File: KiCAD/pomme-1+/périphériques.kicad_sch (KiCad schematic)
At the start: 19 parts, among them J1 DE9_female, J2 5V MCU UART, J3 close to use IRQ on ACIA, J4 rs232-socket, J5 rs232-plug, Q3 2N3904, U10 MAX232CPE

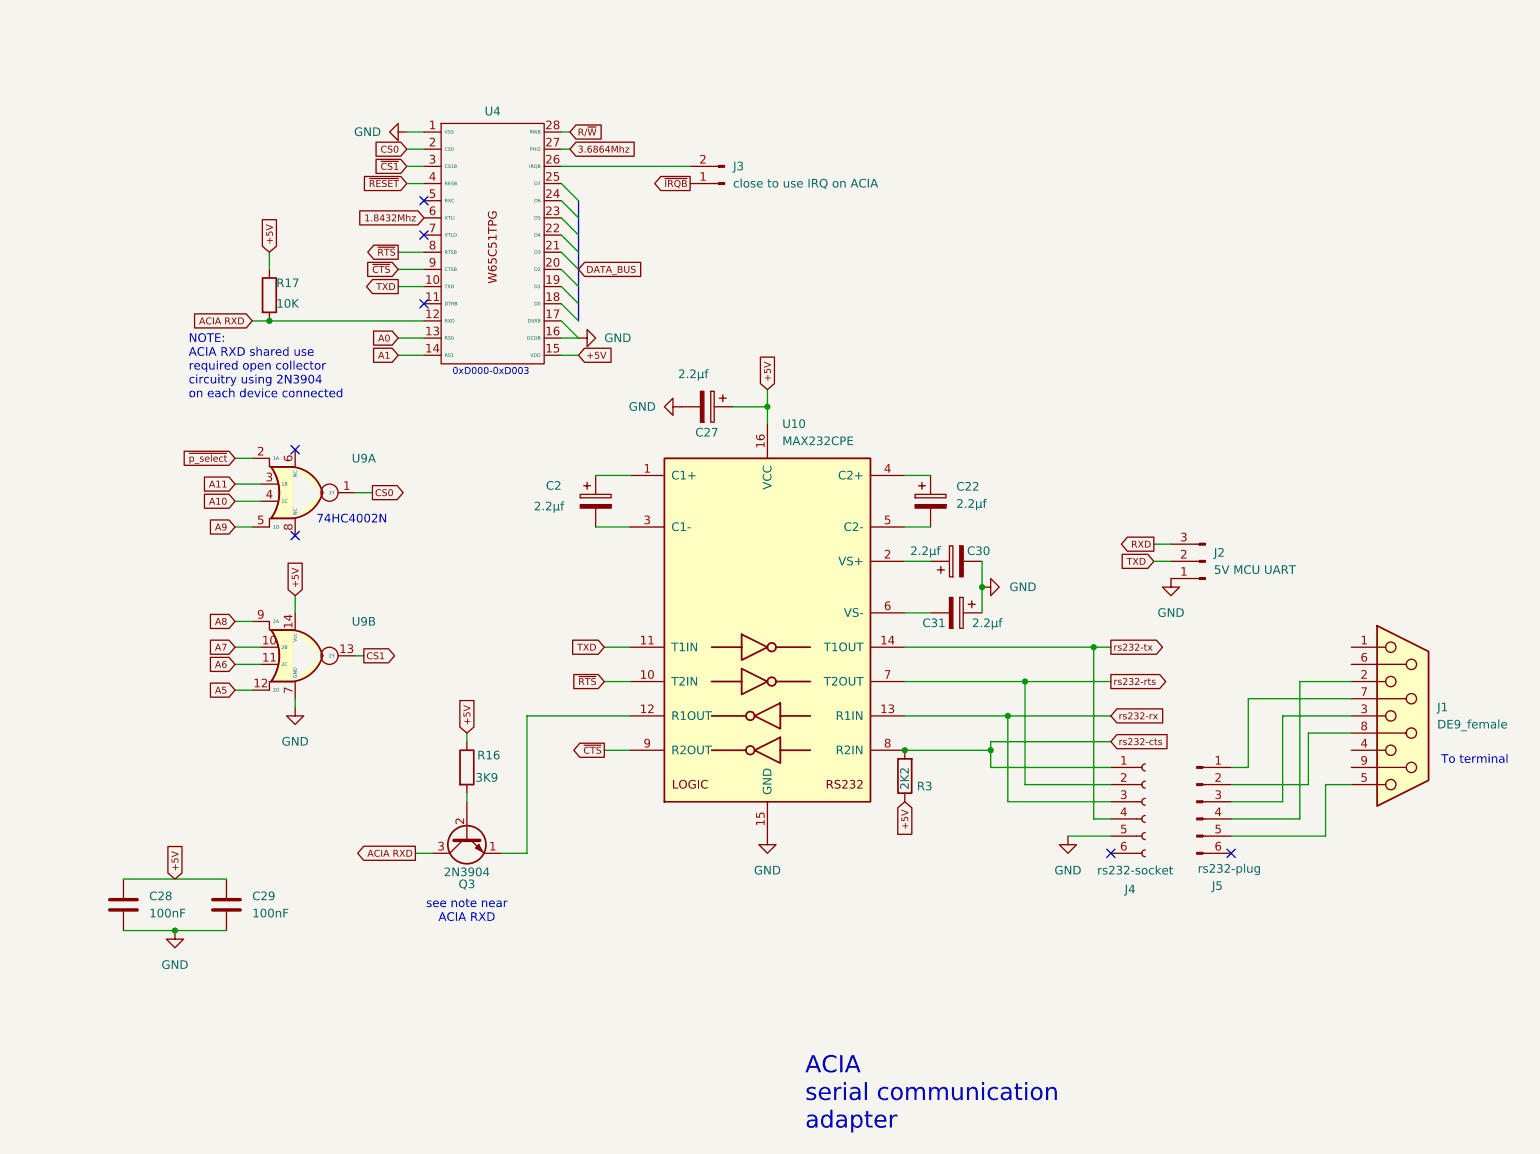
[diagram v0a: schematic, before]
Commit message: Modification de la conception du pomme 1+ Ajout d'un PIA W65C22 à la carte périphériques Ajout d'un régulateur de tension 3.3V à l'alimentation
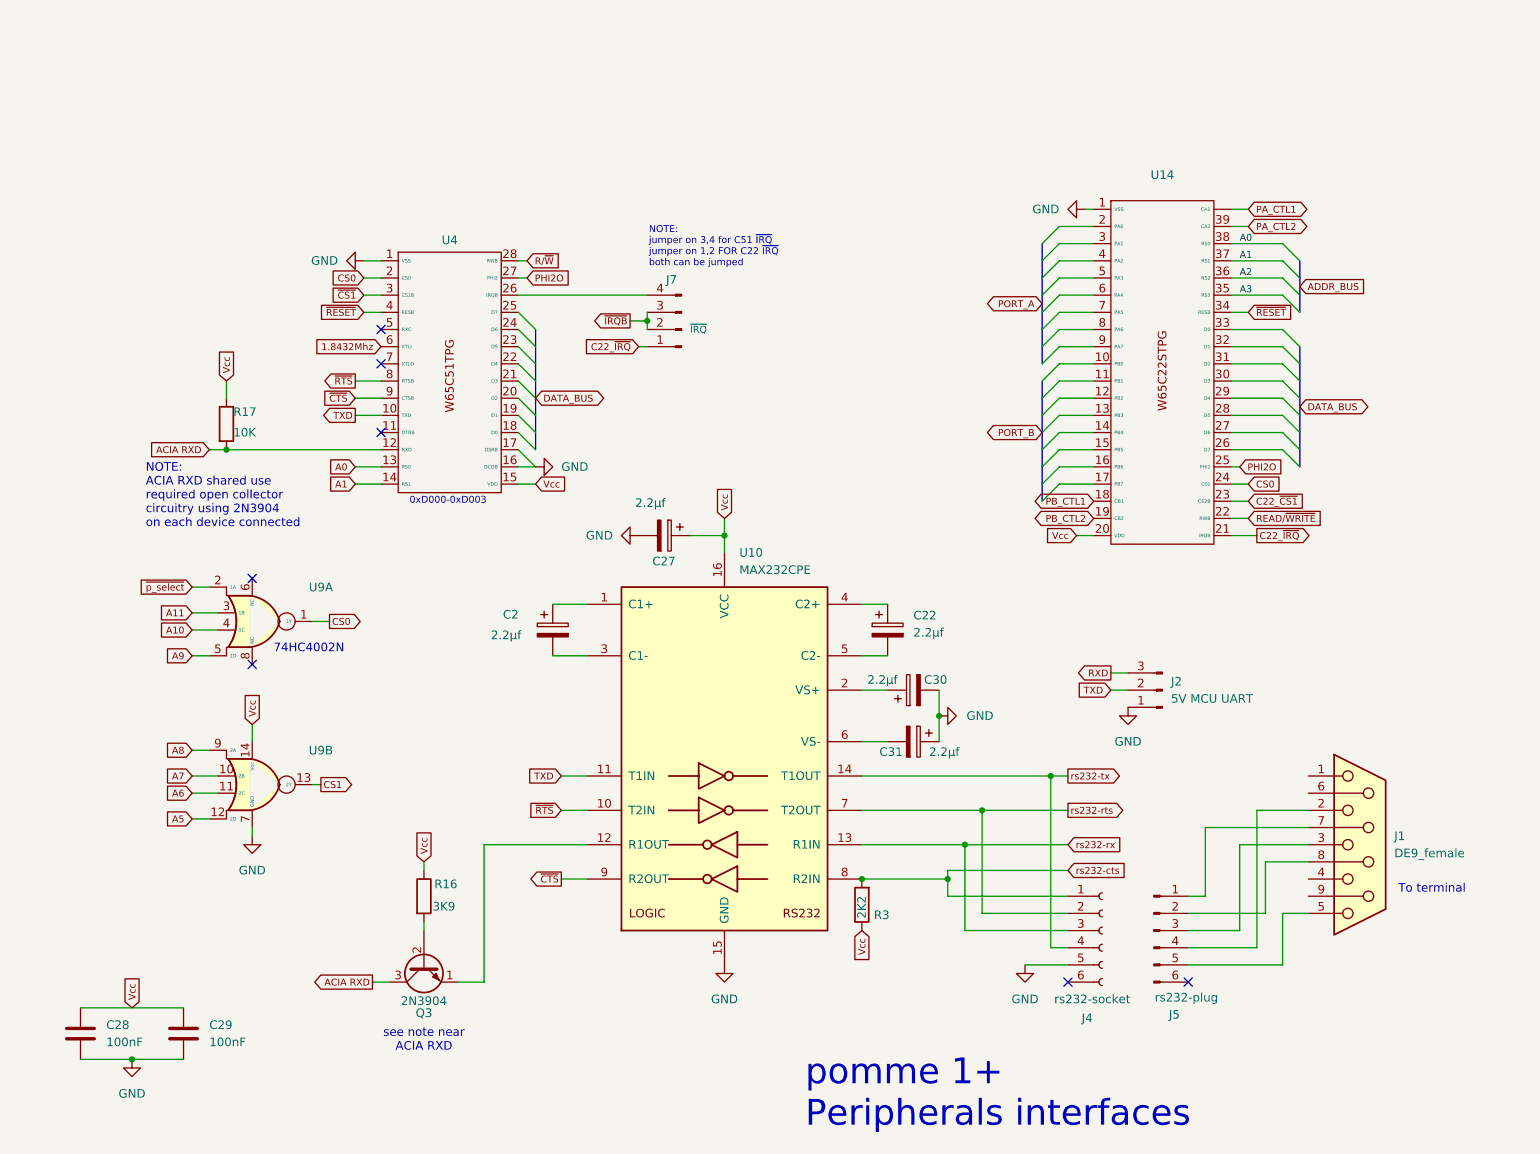
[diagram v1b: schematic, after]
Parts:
- removed J3: close to use IRQ on ACIA, symbol Connector:Conn_01x02_Pin
- added J7: ~{IRQ}, symbol Connector:Conn_01x04_Pin
- added U14: ~, symbol W65Cxx:W65C22STPG
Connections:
- net A0: now also U14.38 (RS0)
- net A1: now also U14.37 (RS1)
- net CS0: now also U14.24 (CS1)
- net GND: now also U14.1 (VSS)
- net ~{IRQB}: now also J7.2 (Pin_2), J7.3 (Pin_3)
- net ~{RESET}: now also U14.34 (RESB)
- net at U4.26 (IRQB): now also J7.4 (Pin_4)
- net +5V renamed Vcc
- net Vcc: now also U14.20 (VDD)
- net 3.6864Mhz renamed PHI2O
- net PHI2O: now also U14.25 (PHI2)
- new net A2: U14.36 (RS2)
- new net A3: U14.35 (RS3)
- new net C22_~{CS1}: U14.23 (CS2B)
- new net C22_~{IRQ}: J7.1 (Pin_1), U14.21 (IRQB)
- new net PA_CTL1: U14. (CA1)
- new net PA_CTL2: U14.39 (CA2)
- new net PB_CTL1: U14.18 (CB1)
- new net PB_CTL2: U14.19 (CB2)
- new net READ/~{WRITE}: U14.22 (RWB)
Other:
- note added: "NOTE: jumper on 3,4 for C51 ~{IRQ} jumper on 1,2 FOR C22 ~{IRQ} both can be jumped"
- note added: "pomme 1+ Peripherals interfaces"
- note removed: "ACIA serial communication adapter"
- moved on the sheet: C2, C22, C27, C28, C29, C30, C31, J1, J2, J4, J5, Q3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

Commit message: Modification documents
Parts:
- renumbered C28 to C19, C29 to C20, C2 to C21, C27 to C22, C22 to C23, C30 to C24, C31 to C25, J7 to J3, J2 to J6, J1 to J7, Q3 to Q1, R17 to R10, R16 to R11, R3 to R12, U14 to U11, U9 to U8, U4 to U9
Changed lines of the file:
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@@
 		(dnp no)
 		(fields_autoplaced yes)
-		(property "Reference" "C22"
+		(property "Reference" "C23"
 			(at 194.31 103.2509 0)
 			(effects
@@
 			(project "pomme-1.5"
 				(path "/46a37b86-f1f5-4cd9-9809-f219c84ab6f2/b95291a5-dff0-4cc1-8588-7d50061f5092"
-					(reference "C22")
+					(reference "C23")
 					(unit 1)
 				)
@@
 		(on_board yes)
 		(dnp no)
-		(property "Reference" "R16"
+		(property "Reference" "R11"
 			(at 123.444 143.002 0)
 			(effects
@@
 			(project ""
 				(path "/46a37b86-f1f5-4cd9-9809-f219c84ab6f2/b95291a5-dff0-4cc1-8588-7d50061f5092"
-					(reference "R16")
+					(reference "R11")
 					(unit 1)
 				)
@@
 		(on_board yes)
 		(dnp no)
-		(property "Reference" "R17"
+		(property "Reference" "R10"
 			(at 93.726 73.152 0)
 			(effects
@@
 			(project ""
 				(path "/46a37b86-f1f5-4cd9-9809-f219c84ab6f2/b95291a5-dff0-4cc1-8588-7d50061f5092"
-					(reference "R17")
+					(reference "R10")
 					(unit 1)
 				)
@@
 		(on_board yes)
 		(dnp no)
-		(property "Reference" "Q3"
+		(property "Reference" "Q1"
 			(at 121.92 162.052 90)
 			(effects
@@
 			(project ""
 				(path "/46a37b86-f1f5-4cd9-9809-f219c84ab6f2/b95291a5-dff0-4cc1-8588-7d50061f5092"
-					(reference "Q3")
+					(reference "Q1")
 					(unit 1)
 				)
@@
 		(dnp no)
 		(fields_autoplaced yes)
-		(property "Reference" "J2"
+		(property "Reference" "J6"
 			(at 232.41 113.0299 0)
 			(effects
@@
 			(project ""
 				(path "/46a37b86-f1f5-4cd9-9809-f219c84ab6f2/b95291a5-dff0-4cc1-8588-7d50061f5092"
-					(reference "J2")
+					(reference "J6")
 					(unit 1)
 				)
@@
 		(dnp no)
 		(fields_autoplaced yes)
-		(property "Reference" "#PWR01"
+		(property "Reference" "#PWR022"
 			(at 166.37 161.29 0)
 			(effects
@@
 			(project "pomme-1.5"
 				(path "/46a37b86-f1f5-4cd9-9809-f219c84ab6f2/b95291a5-dff0-4cc1-8588-7d50061f5092"
-					(reference "#PWR01")
+					(reference "#PWR022")
 					(unit 1)
 				)
@@
 		(dnp no)
 		(fields_autoplaced yes)
-		(property "Reference" "#PWR020"
+		(property "Reference" "#PWR017"
 			(at 78.74 175.26 0)
 			(effects
@@
 			(project "pomme-1.5"
 				(path "/46a37b86-f1f5-4cd9-9809-f219c84ab6f2/b95291a5-dff0-4cc1-8588-7d50061f5092"
-					(reference "#PWR020")
+					(reference "#PWR017")
 					(unit 1)
 				)
@@
 		(on_board yes)
 		(dnp no)
-		(property "Reference" "J7"
+		(property "Reference" "J3"
 			(at 157.734 53.594 0)
 			(effects
@@
 			(project ""
 				(path "/46a37b86-f1f5-4cd9-9809-f219c84ab6f2/b95291a5-dff0-4cc1-8588-7d50061f5092"
-					(reference "J7")
+					(reference "J3")
 					(unit 1)
 				)
@@
 		(on_board yes)
 		(dnp no)
-		(property "Reference" "C30"
+		(property "Reference" "C24"
 			(at 197.612 112.776 90)
 			(effects
@@
 			(project "pomme-1.5"
 				(path "/46a37b86-f1f5-4cd9-9809-f219c84ab6f2/b95291a5-dff0-4cc1-8588-7d50061f5092"
-					(reference "C30")
+					(reference "C24")
 					(unit 1)
 				)
@@
 		(dnp no)
 		(fields_autoplaced yes)
-		(property "Reference" "J1"
+		(property "Reference" "J7"
 			(at 265.43 135.8899 0)
 			(effects
@@
 			(project ""
 				(path "/46a37b86-f1f5-4cd9-9809-f219c84ab6f2/b95291a5-dff0-4cc1-8588-7d50061f5092"
-					(reference "J1")
+					(reference "J7")
 					(unit 1)
 				)
@@
 		(dnp no)
 		(fields_autoplaced yes)
-		(property "Reference" "#PWR022"
+		(property "Reference" "#PWR024"
 			(at 210.82 161.29 0)
 			(effects
@@
 			(project ""
 				(path "/46a37b86-f1f5-4cd9-9809-f219c84ab6f2/b95291a5-dff0-4cc1-8588-7d50061f5092"
-					(reference "#PWR022")
+					(reference "#PWR024")
 					(unit 1)
 				)
@@
 		(dnp no)
 		(fields_autoplaced yes)
-		(property "Reference" "#PWR02"
+		(property "Reference" "#PWR021"
 			(at 147.32 91.44 0)
 			(effects
@@
 			(project "pomme-1.5"
 				(path "/46a37b86-f1f5-4cd9-9809-f219c84ab6f2/b95291a5-dff0-4cc1-8588-7d50061f5092"
-					(reference "#PWR02")
+					(reference "#PWR021")
 					(unit 1)
 				)
@@
 		(dnp no)
 		(fields_autoplaced yes)
-		(property "Reference" "U14"
+		(property "Reference" "U11"
 			(at 231.14 38.1 0)
 			(effects
@@
 			(project ""
 				(path "/46a37b86-f1f5-4cd9-9809-f219c84ab6f2/b95291a5-dff0-4cc1-8588-7d50061f5092"
-					(reference "U14")
+					(reference "U11")
 					(unit 1)
 				)
@@
 		(on_board yes)
 		(dnp no)
-		(property "Reference" "C2"
+		(property "Reference" "C21"
 			(at 133.604 103.124 0)
 			(effects
@@
 			(project ""
 				(path "/46a37b86-f1f5-4cd9-9809-f219c84ab6f2/b95291a5-dff0-4cc1-8588-7d50061f5092"
-					(reference "C2")
+					(reference "C21")
 					(unit 1)
 				)
@@
 		(on_board yes)
 		(dnp no)
-		(property "Reference" "U4"
+		(property "Reference" "U9"
 			(at 125.73 47.752 0)
 			(effects
@@
 			(project "pomme-1.5"
 				(path "/46a37b86-f1f5-4cd9-9809-f219c84ab6f2/b95291a5-dff0-4cc1-8588-7d50061f5092"
-					(reference "U4")
+					(reference "U9")
 					(unit 1)
 				)
@@
 		(on_board yes)
 		(dnp no)
-		(property "Reference" "C31"
+		(property "Reference" "C25"
 			(at 191.008 123.444 90)
 			(effects
@@
 			(project "pomme-1.5"
 				(path "/46a37b86-f1f5-4cd9-9809-f219c84ab6f2/b95291a5-dff0-4cc1-8588-7d50061f5092"
-					(reference "C31")
+					(reference "C25")
 					(unit 1)
 				)
@@
 		(dnp no)
 		(fields_autoplaced yes)
-		(property "Reference" "C29"
+		(property "Reference" "C20"
 			(at 90.17 163.8299 0)
 			(effects
@@
 			(project ""
 				(path "/46a37b86-f1f5-4cd9-9809-f219c84ab6f2/b95291a5-dff0-4cc1-8588-7d50061f5092"
-					(reference "C29")
+					(reference "C20")
 					(unit 1)
 				)
@@
 		(dnp no)
 		(fields_autoplaced yes)
-		(property "Reference" "C28"
+		(property "Reference" "C19"
 			(at 74.93 163.8299 0)
 			(effects
@@
 			(project ""
 				(path "/46a37b86-f1f5-4cd9-9809-f219c84ab6f2/b95291a5-dff0-4cc1-8588-7d50061f5092"
-					(reference "C28")
+					(reference "C19")
 					(unit 1)
 				)
@@
 		(dnp no)
 		(fields_autoplaced yes)
-		(property "Reference" "#PWR012"
+		(property "Reference" "#PWR020"
 			(at 144.78 81.28 0)
 			(effects
@@
 			(project "pomme-1.5"
 				(path "/46a37b86-f1f5-4cd9-9809-f219c84ab6f2/b95291a5-dff0-4cc1-8588-7d50061f5092"
-					(reference "#PWR012")
+					(reference "#PWR020")
 					(unit 1)
 				)
@@
 		(dnp no)
 		(fields_autoplaced yes)
-		(property "Reference" "#PWR06"
+		(property "Reference" "#PWR018"
 			(at 96.52 142.24 0)
 			(effects
@@
 			(project "pomme-1.5"
 				(path "/46a37b86-f1f5-4cd9-9809-f219c84ab6f2/b95291a5-dff0-4cc1-8588-7d50061f5092"
-					(reference "#PWR06")
+					(reference "#PWR018")
 					(unit 1)
 				)
@@
 		(on_board yes)
 		(dnp no)
-		(property "Reference" "C27"
+		(property "Reference" "C22"
 			(at 155.702 95.25 90)
 			(effects
@@
 			(project "pomme-1.5"
 				(path "/46a37b86-f1f5-4cd9-9809-f219c84ab6f2/b95291a5-dff0-4cc1-8588-7d50061f5092"
-					(reference "C27")
+					(reference "C22")
 					(unit 1)
 				)
@@
 		(dnp no)
 		(fields_autoplaced yes)
-		(property "Reference" "U9"
+		(property "Reference" "U8"
 			(at 106.68 99.0914 0)
 			(effects
@@
 			(project ""
 				(path "/46a37b86-f1f5-4cd9-9809-f219c84ab6f2/b95291a5-dff0-4cc1-8588-7d50061f5092"
-					(reference "U9")
+					(reference "U8")
 					(unit 1)
 				)
@@
 		(dnp no)
 		(fields_autoplaced yes)
-		(property "Reference" "U9"
+		(property "Reference" "U8"
 			(at 106.68 123.2214 0)
 			(effects
@@
 			(project ""
 				(path "/46a37b86-f1f5-4cd9-9809-f219c84ab6f2/b95291a5-dff0-4cc1-8588-7d50061f5092"
-					(reference "U9")
+					(reference "U8")
 					(unit 2)
 				)
@@
 		(on_board yes)
 		(dnp no)
-		(property "Reference" "R3"
+		(property "Reference" "R12"
 			(at 188.468 147.574 0)
 			(effects
@@
 			(project ""
 				(path "/46a37b86-f1f5-4cd9-9809-f219c84ab6f2/b95291a5-dff0-4cc1-8588-7d50061f5092"
-					(reference "R3")
+					(reference "R12")
 					(unit 1)
 				)
@@
 		(dnp no)
 		(fields_autoplaced yes)
-		(property "Reference" "#PWR023"
+		(property "Reference" "#PWR026"
 			(at 226.06 123.19 0)
 			(effects
@@
 			(project "pomme-1.5"
 				(path "/46a37b86-f1f5-4cd9-9809-f219c84ab6f2/b95291a5-dff0-4cc1-8588-7d50061f5092"
-					(reference "#PWR023")
+					(reference "#PWR026")
 					(unit 1)
 				)
@@
 		(dnp no)
 		(fields_autoplaced yes)
-		(property "Reference" "#PWR028"
+		(property "Reference" "#PWR025"
 			(at 213.36 43.18 0)
 			(effects
@@
 			(project ""
 				(path "/46a37b86-f1f5-4cd9-9809-f219c84ab6f2/b95291a5-dff0-4cc1-8588-7d50061f5092"
-					(reference "#PWR028")
+					(reference "#PWR025")
 					(unit 1)
 				)
@@
 		(dnp no)
 		(fields_autoplaced yes)
-		(property "Reference" "#PWR03"
+		(property "Reference" "#PWR019"
 			(at 106.68 50.8 0)
 			(effects
@@
 			(project "pomme-1.5"
 				(path "/46a37b86-f1f5-4cd9-9809-f219c84ab6f2/b95291a5-dff0-4cc1-8588-7d50061f5092"
-					(reference "#PWR03")
+					(reference "#PWR019")
 					(unit 1)
 				)
@@
 		(dnp no)
 		(fields_autoplaced yes)
-		(property "Reference" "#PWR021"
+		(property "Reference" "#PWR023"
 			(at 204.47 118.11 0)
 			(effects
@@
 			(project "pomme-1.5"
 				(path "/46a37b86-f1f5-4cd9-9809-f219c84ab6f2/b95291a5-dff0-4cc1-8588-7d50061f5092"
-					(reference "#PWR021")
-					(unit 1)
-				)
+					(reference "#PWR023")
+					(unit 1)
+				)
